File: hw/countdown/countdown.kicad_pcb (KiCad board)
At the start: 4 copper layers, 44 x 22 mm, 24 parts, among them J1 TC2030-SWD, SW1 TS-1187A-B-A-B, U1 STM32L031G6U6, Y1 32.768kHz

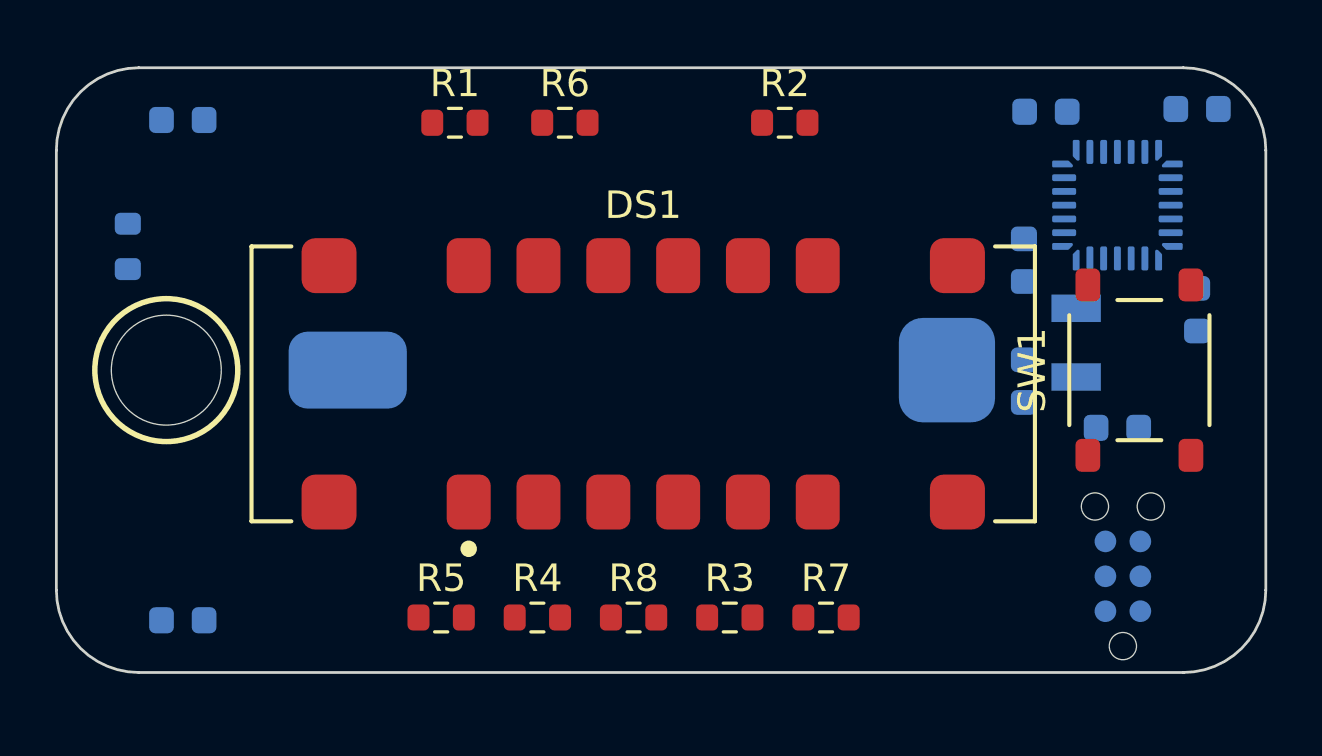
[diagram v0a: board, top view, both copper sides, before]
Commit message: Routing infrastructure: plain-DSN freerouting flow + deterministic 4-layer repair router
Co-Authored-By: Claude Fable 5 <noreply@anthropic.com>
Claude-Session: https://claude.ai/code/session_01EyK7WVGPpPEnSjWLWWV8on
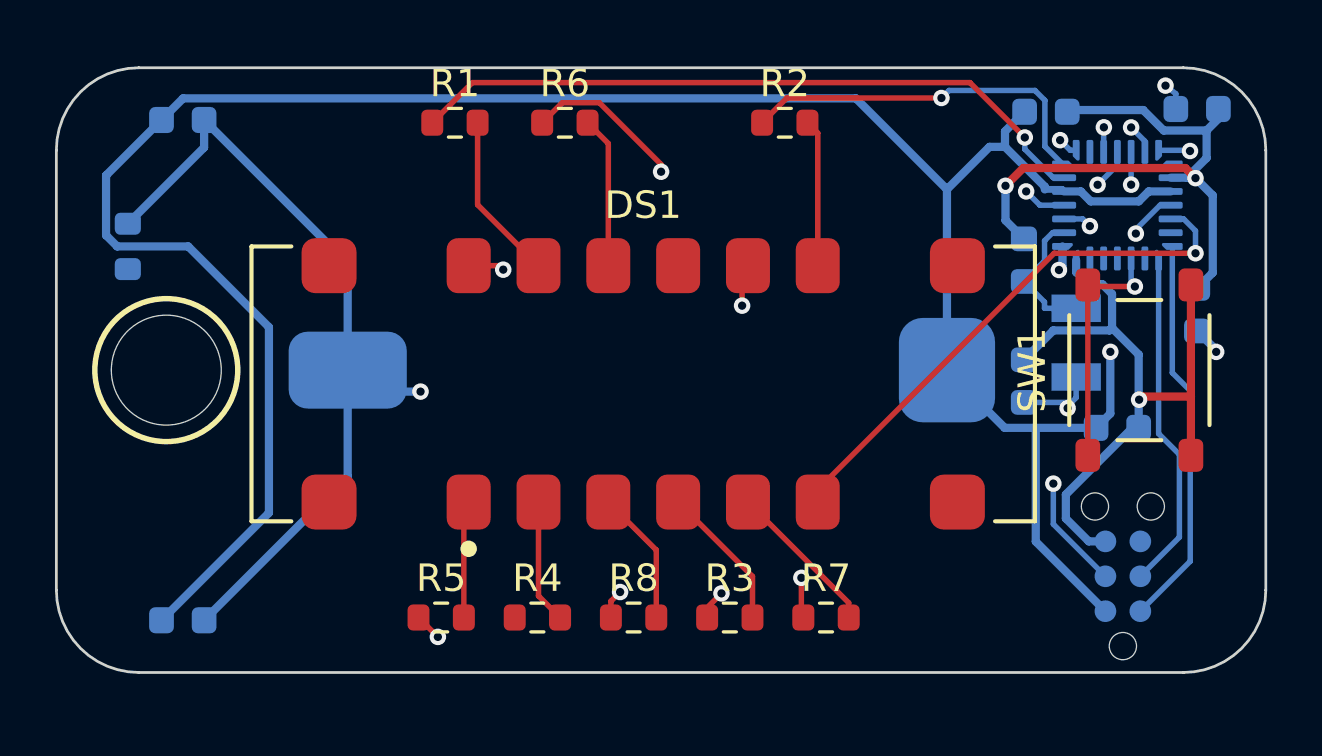
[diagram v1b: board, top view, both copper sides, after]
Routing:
- net GND: track 0.00 -> 114.0 mm, vias 0 -> 4
- net VDD: track 0.00 -> 99.4 mm, vias 0 -> 3
- net SEG_E: track 0.00 -> 34.0 mm, vias 0 -> 2
- net SEG_C: track 0.00 -> 33.6 mm, vias 0 -> 2
- net NRST: track 0.00 -> 31.8 mm, vias 0 -> 3
- net DIG_1: track 0.00 -> 29.2 mm, vias 0 -> 2
- net SEG_DP: track 0.00 -> 27.8 mm, vias 0 -> 2
- net SEG_A: track 0.00 -> 25.3 mm, vias 0 -> 1
- net SEG_F: track 0.00 -> 23.5 mm, vias 0 -> 2
- net SEG_G: track 0.00 -> 22.4 mm, vias 0 -> 2
- net DIG_4: track 0.00 -> 19.7 mm, vias 0 -> 1
- net DIG_3: track 0.00 -> 18.7 mm, vias 0 -> 2
- net SWDIO: track 0.00 -> 14.3 mm
- net SEG_B: track 0.00 -> 13.5 mm, vias 0 -> 1
- net SWCLK: track 0.00 -> 12.4 mm
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
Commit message: Freerouting-free routing flow (A* with power-first fanout), firmware cleanup, JLC rotation research
Co-Authored-By: Claude Fable 5 <noreply@anthropic.com>
Claude-Session: https://claude.ai/code/session_01EyK7WVGPpPEnSjWLWWV8on
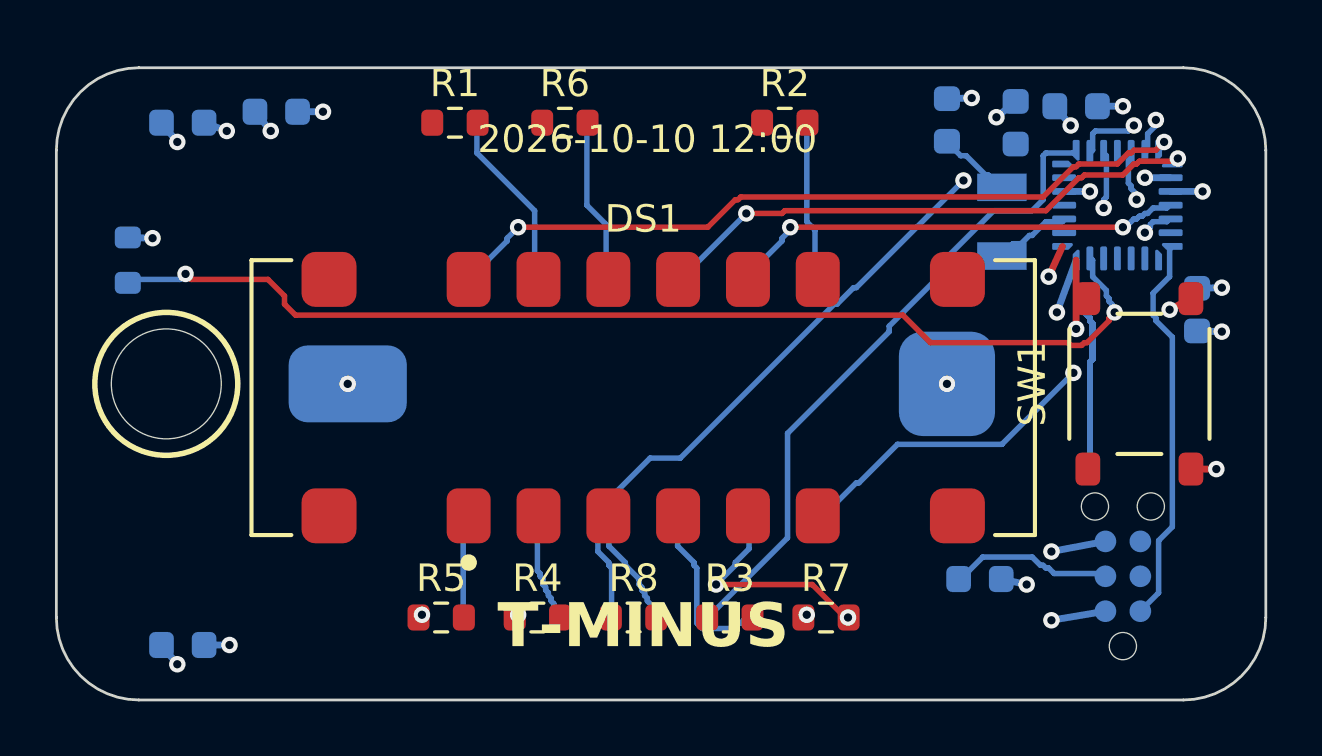
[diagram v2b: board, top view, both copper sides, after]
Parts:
- moved C4 32.7 mm to (8.00, 1.60)
- moved C3 18.8 mm to (33.6, 18.6)
- moved C8 9.40 mm to (34.9, 2.00)
- moved C7 5.82 mm to (32.4, 1.90)
- moved Y1 5.16 mm to (34.4, 5.60)
- moved C2 1.12 mm to (37.1, 1.40)
- moved C6 0.90 mm to (4.60, 21.0)
- moved BT1 0.50 mm to (19.4, 11.5)
- moved DS1 0.50 mm to (21.4, 12.0)
- moved H1 0.50 mm to (4.00, 11.5)
- moved R9 0.50 mm to (2.60, 7.00)
- moved SW1 0.50 mm to (39.4, 11.5)
- moved C5 0.10 mm to (4.60, 2.00)
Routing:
- net VDD: track 99.4 -> 9.83 mm, vias 3 -> 10
- net BOOT0: track 0.00 -> 40.3 mm, vias 0 -> 2
- net SEG_D: track 0.00 -> 32.3 mm, vias 0 -> 2
- net GND: track 114.0 -> 142.3 mm, vias 4 -> 15
- net NRST: track 31.8 -> 6.08 mm, vias 3 -> 0
- net SEG_A: track 25.3 -> 0.00 mm, vias 1 -> 0
- net SEG_F: track 23.5 -> 0.00 mm, vias 2 -> 0
- net DIG_2: track 0.00 -> 20.3 mm, vias 0 -> 2
- net SEG_B: track 13.5 -> 0.00 mm, vias 1 -> 0
- net SWCLK: track 12.4 -> 0.00 mm
- net SEG_C: track 33.6 -> 24.0 mm, vias 2 -> 0
- net LSE_OUT: track 12.2 -> 2.93 mm, vias 2 -> 0
- net BTN: track 8.99 -> 2.50 mm
- net SEG_DP: track 27.8 -> 31.9 mm
- net LED_G: track 5.72 -> 8.36 mm, vias 0 -> 2
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- added copper zone on In1.Cu, net GND
- added copper zone on In2.Cu, net VDD
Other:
- board size 44 x 22 mm -> 44 x 23 mm
- board text added: "2026-10-10 12:00"
- board text added: "COUNTDOWN v1 2026"
- board text added: "T-MINUS"

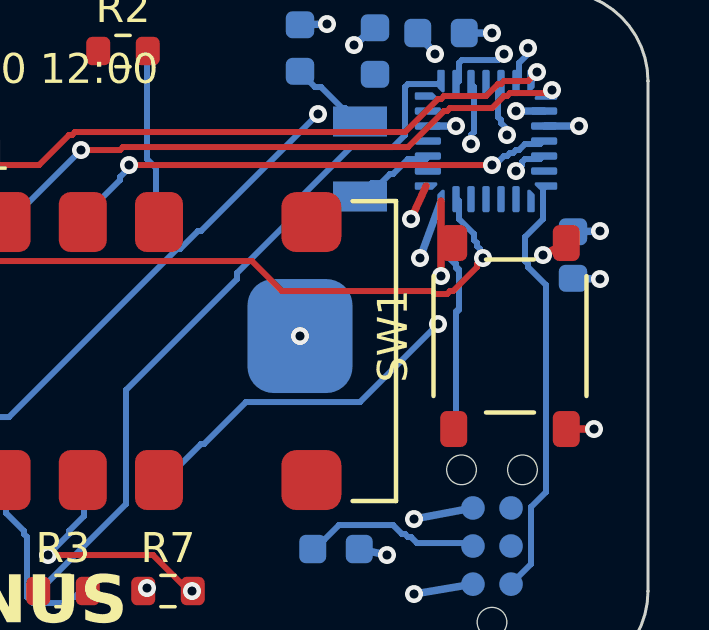
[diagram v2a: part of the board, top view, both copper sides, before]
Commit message: README + JLCPCB ordering guide
Co-Authored-By: Claude Fable 5 <noreply@anthropic.com>
Claude-Session: https://claude.ai/code/session_01EyK7WVGPpPEnSjWLWWV8on
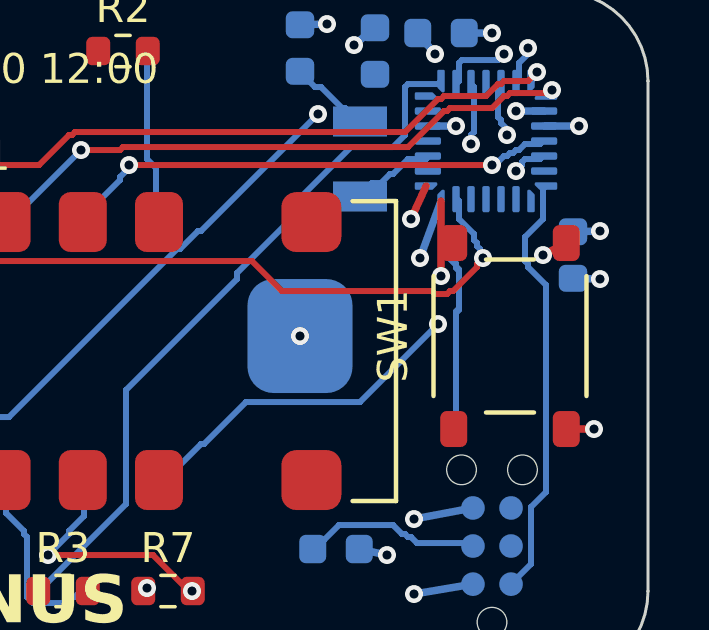
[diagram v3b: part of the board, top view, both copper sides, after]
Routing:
- net GND: track 142.3 -> 166.2 mm

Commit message: Design log: routing endgame narrative
Co-Authored-By: Claude Fable 5 <noreply@anthropic.com>
Claude-Session: https://claude.ai/code/session_01EyK7WVGPpPEnSjWLWWV8on
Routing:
- net GND: track 166.2 -> 182.1 mm

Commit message: Prompt log updates
Co-Authored-By: Claude Fable 5 <noreply@anthropic.com>
Claude-Session: https://claude.ai/code/session_01EyK7WVGPpPEnSjWLWWV8on
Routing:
- net GND: track 182.1 -> 213.9 mm

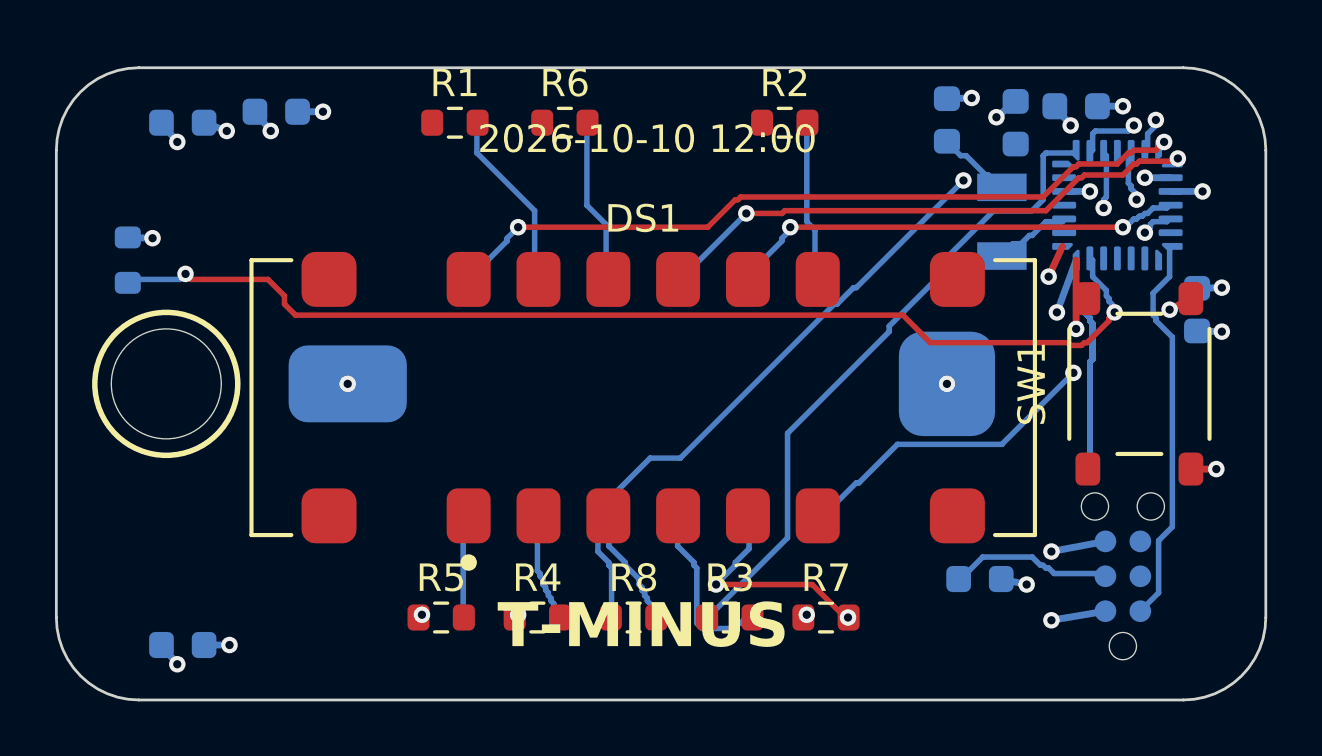
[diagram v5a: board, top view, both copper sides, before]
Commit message: Review fixes (fw: BYPSHAD, LSEDRV order, flash staleness, vectors; sch: diagonal switch wiring) + routing endgame tooling
Co-Authored-By: Claude Fable 5 <noreply@anthropic.com>
Claude-Session: https://claude.ai/code/session_01EyK7WVGPpPEnSjWLWWV8on
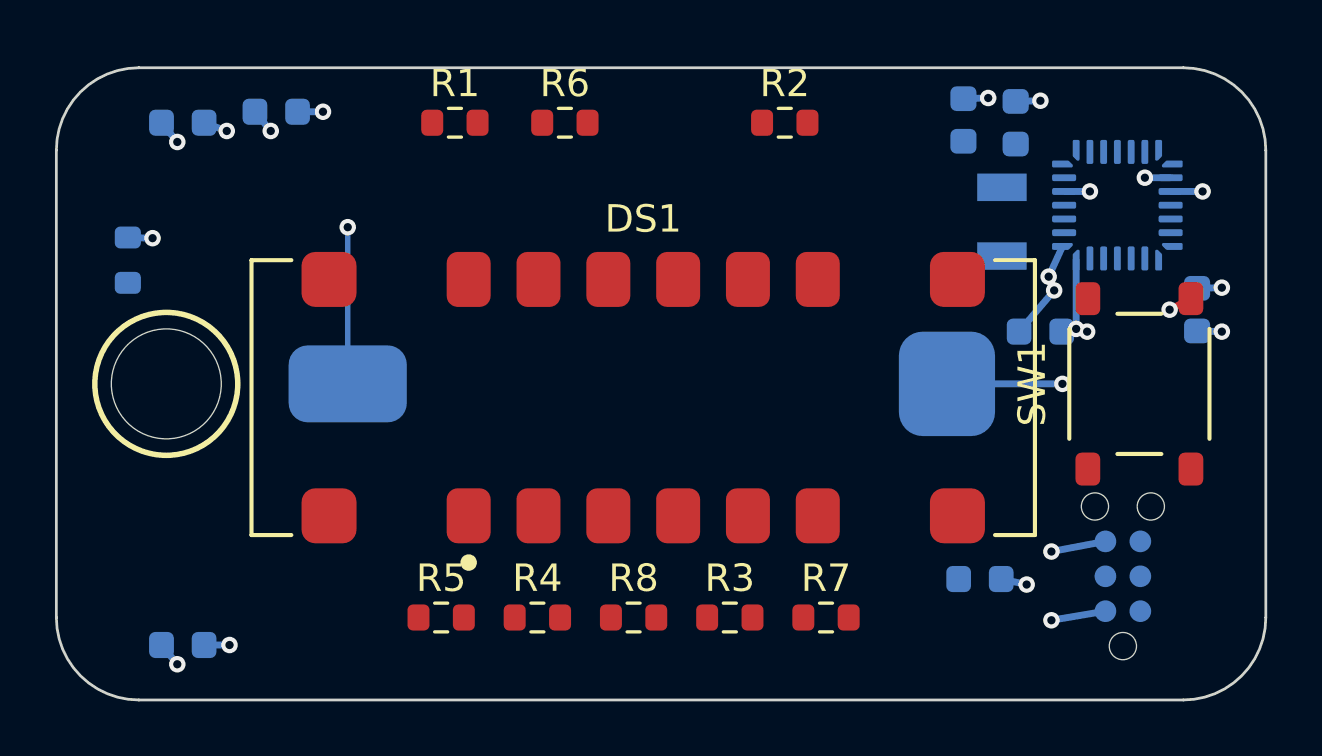
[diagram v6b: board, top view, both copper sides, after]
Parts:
- moved C2 8.30 mm to (35.8, 9.60)
- moved C7 0.60 mm to (33.0, 1.90)
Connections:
- SW1 pad 2: BTN -> unconnected-(SW1-B-Pad2)
- SW1 pad 3: GND -> unconnected-(SW1-C-Pad3)
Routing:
- net GND: track 213.9 -> 20.2 mm, vias 15 -> 14
- net BOOT0: track 40.3 -> 0.00 mm, vias 2 -> 0
- net SEG_E: track 33.2 -> 0.00 mm, vias 2 -> 0
- net SEG_D: track 32.3 -> 0.00 mm, vias 2 -> 0
- net SEG_DP: track 31.9 -> 0.00 mm, vias 2 -> 0
- net DIG_1: track 27.8 -> 0.00 mm, vias 2 -> 0
- net SEG_C: track 24.0 -> 0.00 mm
- net SEG_G: track 23.1 -> 0.00 mm, vias 2 -> 0
- net DIG_2: track 20.3 -> 0.00 mm, vias 2 -> 0
- net DIG_4: track 18.8 -> 0.00 mm, vias 2 -> 0
- net DIG_3: track 16.7 -> 0.00 mm, vias 2 -> 0
- net SWDIO: track 14.4 -> 0.00 mm
- net LED_G: track 8.36 -> 0.00 mm, vias 2 -> 0
- net LED_A: track 6.68 -> 0.00 mm
- net LED_C: track 6.48 -> 0.00 mm
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- removed copper zone on In1.Cu, net GND
- removed copper zone on In2.Cu, net VDD
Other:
- board text removed: "2026-10-10 12:00"
- board text removed: "COUNTDOWN v1 2026"
- board text removed: "T-MINUS"

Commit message: Design log review outcomes; ordering doc updates
Co-Authored-By: Claude Fable 5 <noreply@anthropic.com>
Claude-Session: https://claude.ai/code/session_01EyK7WVGPpPEnSjWLWWV8on
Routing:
- net GND: track 20.2 -> 164.1 mm
- net VDD: track 15.1 -> 158.6 mm
- net SEG_DP: track 0.00 -> 83.0 mm, vias 0 -> 2
- net SEG_E: track 0.00 -> 66.2 mm, vias 0 -> 2
- net BOOT0: track 0.00 -> 63.9 mm, vias 0 -> 2
- net SEG_G: track 0.00 -> 54.1 mm, vias 0 -> 2
- net DIG_1: track 0.00 -> 52.9 mm, vias 0 -> 2
- net SEG_F: track 0.00 -> 46.2 mm, vias 0 -> 2
- net SEG_C: track 0.00 -> 41.1 mm, vias 0 -> 2
- net NRST: track 0.00 -> 36.6 mm, vias 0 -> 2
- net DIG_4: track 0.00 -> 36.1 mm, vias 0 -> 1
- net SEG_A: track 0.00 -> 30.0 mm, vias 0 -> 2
- net DIG_2: track 0.00 -> 29.2 mm, vias 0 -> 2
- net SWDIO: track 0.00 -> 26.8 mm
- net SWCLK: track 0.00 -> 24.3 mm
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- added copper zone on In1.Cu, net GND
- added copper zone on In2.Cu, net VDD
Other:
- board text added: "2026-10-10 12:00"
- board text added: "COUNTDOWN v1 2026"
- board text added: "T-MINUS"
